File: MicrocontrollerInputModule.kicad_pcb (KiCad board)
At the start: 2 copper layers, 33.8 x 131 mm, 359 parts, among them J1 Conn_02x04_Odd_Even, SW1 KXT3, SW2 KXT3, U1 W25Q16JVUXIQ, U2 RP2040, U3 TXB0108DQSR, U4 TXB0108DQSR, Y1 12.000MHz

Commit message: Add files via upload
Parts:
- removed the G*** at (73.0, 68.0)
- added G***: LOGO, InputModule:heart, B.Cu at (67.0, 178.9)
- moved C15 13.0 mm to (54.8, 148.8), turned to 90 degrees
- moved R4 12.5 mm to (65.2, 144.2), turned to 0 degrees
- moved C19 12.2 mm to (56.9, 144.3), turned to -90 degrees
- moved R9 6.91 mm to (59.9, 139.2), turned to 45 degrees
- moved G*** 6.40 mm to (72.9, 78.6)
- moved G*** 4.30 mm to (72.9, 105.7)
- moved R8 3.94 mm to (58.6, 153.4)
- moved C20 3.79 mm to (62.6, 140.9)
- moved C17 2.54 mm to (60.7, 154.5), turned to -90 degrees
- moved D2 0.60 mm to (68.0, 153.2), turned to -135 degrees
- moved C14 0.17 mm to (65.2, 146.2)
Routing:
- net /BOARD_ID: track 41.9 -> 22.1 mm, vias 2 -> 3
- net +5V: track 35.8 -> 50.6 mm, vias 19 -> 21
- net /~{RESET}: track 60.4 -> 48.9 mm, vias 2 -> 1
- net GND: track 1066.5 -> 1077.0 mm, vias 103 -> 116
- net Net-(U4-OE): track 13.6 -> 4.24 mm, vias 2 -> 0
- net Net-(R1-Pad1): track 24.4 -> 16.4 mm
- net +3V3: track 112.4 -> 116.7 mm, vias 6 -> 4
- net Net-(U3-OE): track 5.81 -> 1.60 mm, vias 2 -> 0
- net /XIN: track 8.07 -> 10.1 mm
- net Net-(N261-DOUT): track 39.5 -> 37.9 mm
- net /D8: track 16.6 -> 15.4 mm
- net /NeopixelMatrix/STRIP16: track 8.28 -> 7.54 mm
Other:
- board text added: "LED Strip RP2040 Pin Guide:"
- board text added: "LED Strip | GPIO Pin 1 | D23 2 | D22 3 | D21 4 | D17 5 | D16 6 | D15 7 | D14 8 | D13"
- board text added: "LED Strip | GPIO Pin 9 | D12 10 | D11 11 | D10 12 | D9 13 | D8 14 | D7 15 | D6 16 | D5"
- board text added: "LGBTQIA+"
- board text removed: "Check out the Young Amateurs Radio Club for a safe space to learn and experiment with amateur radio!"

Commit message: Version 2
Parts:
- removed C19, C20: 0.1uF, Capacitor_SMD:C_0603_1608Metric
- removed H1, H2: 24929, InputModule:MountingHole_3.7mm_Pad_24929
- removed H3, H4: MountingHole, MountingHole:MountingHole_2.1mm
- removed J1: Conn_02x04_Odd_Even, InputModule:PogoPads_2x4_P2.0mm
- added F1: Polyfuse 600mA, Resistor_SMD:R_1206_3216Metric, B.Cu at (102.9, 149.0)
- added F2: Polyfuse 200mA, Resistor_SMD:R_1206_3216Metric, B.Cu at (110.3, 153.1)
- added J2: FH34SRJ-12S-0.5SH_50_, FH34SRJ-12S-0.5SH_50_:HRS_FH34SRJ-12S-0.5SH_50_, B.Cu at (103.2, 152.5)
- added R10: 470, Resistor_SMD:R_0402_1005Metric, B.Cu at (95.4, 137.0)
- added R11: 470, Resistor_SMD:R_0402_1005Metric, B.Cu at (94.8, 139.6)
- added R12: 470, Resistor_SMD:R_0402_1005Metric, B.Cu at (92.2, 142.1)
- added R13: 470, Resistor_SMD:R_0402_1005Metric, B.Cu at (91.2, 146.7)
- added R14: 470, Resistor_SMD:R_0402_1005Metric, B.Cu at (94.9, 147.6)
- added R15: 470, Resistor_SMD:R_0402_1005Metric, B.Cu at (94.9, 150.0)
- added R16: 470, Resistor_SMD:R_0402_1005Metric, B.Cu at (92.2, 152.0)
- added R17: 0, Resistor_SMD:R_0402_1005Metric, F.Cu at (117.2, 61.3)
- added R18: 0, Resistor_SMD:R_0402_1005Metric, F.Cu at (117.2, 74.9)
- added R19: 0, Resistor_SMD:R_0402_1005Metric, F.Cu at (117.3, 88.6)
- added R20: 0, Resistor_SMD:R_0402_1005Metric, F.Cu at (117.2, 102.3)
- added R21: 0, Resistor_SMD:R_0402_1005Metric, F.Cu at (117.2, 116.1)
- added R22: 0, Resistor_SMD:R_0402_1005Metric, F.Cu at (117.2, 129.8)
- added R23: 0, Resistor_SMD:R_0402_1005Metric, F.Cu at (117.2, 143.5)
- added R24: 10k, Resistor_SMD:R_0402_1005Metric, B.Cu at (109.7, 146.0)
- C17, C18: value 0.1uF -> 10uF
- C21, C22, C23, C24, C25, C26, C27, C28, C29, C30, C31, C32, C33, C34, C35, C36: footprint Capacitor_SMD:C_0402_1005Metric -> Capacitor_SMD:C_0603_1608Metric
- R8: value 10K -> 10k
- R9: value 10K -> 470
- SW1, SW2: moved to B.Cu
- U3, U4: value TXB0108DQSR -> 74AHC125BQ_115; footprint FootprintLibrary:USON-20_2x4mm_P0.4mm -> 74AHC125BQ_115:QFN50P300X250X100-15N
- moved G*** 145.2 mm to (209.6, 151.6)
- moved G*** 145.2 mm to (203.6, 139.7)
- moved G*** 145.2 mm to (194.6, 139.7)
- moved G*** 145.2 mm to (215.6, 100.7)
- moved G*** 145.2 mm to (200.6, 139.7)
- moved G*** 145.2 mm to (197.6, 139.7)
- moved G*** 145.2 mm to (206.9, 140.1)
- moved G*** 111.2 mm to (176.6, 65.7)
- moved G*** 108.5 mm to (176.6, 46.7)
- moved C15 51.9 mm to (106.7, 149.4), turned to 0 degrees
- moved SW2 51.8 mm to (100.5, 136.9), turned to 0 degrees
- moved R8 50.1 mm to (108.2, 146.4), turned to 90 degrees
- moved SW1 44.2 mm to (115.2, 149.8), turned to 90 degrees
- moved C1 40.7 mm to (102.3, 142.5), turned to 180 degrees
- moved C9 39.6 mm to (116.0, 140.5)
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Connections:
- C17 pad 1: +3V3 -> +5V
- C18 pad 1: GND -> +5V
- C18 pad 2: +5V -> GND
- N127 pad 4: /NeopixelMatrix/STRIP8 -> /NeopixelMatrix/END-STRIP7
- N163 pad 4: /NeopixelMatrix/STRIP10 -> /NeopixelMatrix/END-STRIP19
- N19 pad 4: /NeopixelMatrix/STRIP2 -> /NeopixelMatrix/END-STRIP1
- N199 pad 4: /NeopixelMatrix/STRIP12 -> /NeopixelMatrix/END-STRIP11
- N235 pad 4: /NeopixelMatrix/STRIP14 -> /NeopixelMatrix/END-STRIP13
- N271 pad 4: /NeopixelMatrix/STRIP16 -> /NeopixelMatrix/END-STRIP15
- N55 pad 4: /NeopixelMatrix/STRIP4 -> /NeopixelMatrix/END-STRIP3
- N91 pad 4: /NeopixelMatrix/STRIP6 -> /NeopixelMatrix/END-STRIP5
- R8 pad 1: Net-(U3-OE) -> GND
- R8 pad 2: +3V3 -> /D7
- R9 pad 1: Net-(U4-OE) -> Net-(U3-1Y)
- R9 pad 2: +3V3 -> /NeopixelMatrix/STRIP1
- U2 pad 27: /D16 -> unconnected-(U2-GPIO16-Pad27)
- U2 pad 28: /D17 -> unconnected-(U2-GPIO17-Pad28)
- U2 pad 32: /D21 -> unconnected-(U2-GPIO21-Pad32)
- U2 pad 34: /D22 -> unconnected-(U2-GPIO22-Pad34)
- U2 pad 35: /D23 -> unconnected-(U2-GPIO23-Pad35)
- U2 pad 7: /D5 -> unconnected-(U2-GPIO5-Pad7)
- U2 pad 8: /D6 -> Net-(U2-GPIO6)
- U3 pad 1: /D12 -> Net-(U2-GPIO6)
- U3 pad 10: /D5 -> /D7
- U3 pad 11: /NeopixelMatrix/STRIP16 -> Net-(U3-4Y)
- U3 pad 12: /NeopixelMatrix/STRIP15 -> /D12
- U3 pad 13: /NeopixelMatrix/STRIP14 -> /D7
- U3 pad 14: /NeopixelMatrix/STRIP13 -> +5V
- U3 pad 2: /D11 -> /D15
- U3 pad 3: /D10 -> Net-(U3-1Y)
- U3 pad 4: /D9 -> /D7
- U3 pad 5: +3V3 -> /D14
- U3 pad 6: Net-(U3-OE) -> Net-(U3-2Y)
- U3 pad 7: /D8 -> GND
- U3 pad 8: /D7 -> Net-(U3-3Y)
- U3 pad 9: /D6 -> /D13
- U4 pad 1: /D23 -> /D7
- U4 pad 10: /D13 -> /D7
- U4 pad 11: /NeopixelMatrix/STRIP8 -> Net-(U4-4Y)
- U4 pad 12: /NeopixelMatrix/STRIP7 -> /D8
- U4 pad 13: /NeopixelMatrix/STRIP6 -> /D7
- U4 pad 14: /NeopixelMatrix/STRIP5 -> +5V
- U4 pad 2: /D22 -> /D11
- U4 pad 3: /D21 -> Net-(U4-1Y)
- U4 pad 4: /D17 -> /D7
- U4 pad 5: +3V3 -> /D10
- U4 pad 6: Net-(U4-OE) -> Net-(U4-2Y)
- U4 pad 7: /D16 -> GND
- U4 pad 8: /D15 -> Net-(U4-3Y)
- U4 pad 9: /D14 -> /D9
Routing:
- net /NeopixelMatrix/STRIP2: track 81.1 -> 0.00 mm, vias 1 -> 0
- net /NeopixelMatrix/STRIP4: track 66.6 -> 0.00 mm, vias 1 -> 0
- net Net-(U2-GPIO6): track 0.00 -> 55.4 mm, vias 0 -> 2
- net +3V3: track 116.7 -> 61.7 mm, vias 4 -> 0
- net /NeopixelMatrix/STRIP6: track 50.9 -> 0.00 mm, vias 1 -> 0
- net /~{RESET}: track 48.9 -> 4.24 mm, vias 1 -> 0
- net +5V: track 50.6 -> 7.03 mm, vias 21 -> 1
- net /NeopixelMatrix/STRIP7: track 44.4 -> 87.5 mm
- net /NeopixelMatrix/STRIP5: track 58.5 -> 99.9 mm, vias 1 -> 3
- net /NeopixelMatrix/STRIP11: track 28.9 -> 66.2 mm, vias 1 -> 5
- net /NeopixelMatrix/STRIP8: track 36.9 -> 0.00 mm, vias 1 -> 0
- net /NeopixelMatrix/STRIP15: track 4.15 -> 41.0 mm, vias 1 -> 3
- net /NeopixelMatrix/STRIP10: track 35.6 -> 0.00 mm, vias 1 -> 0
- net /NeopixelMatrix/STRIP3: track 73.9 -> 108.0 mm, vias 1 -> 3
- net /NeopixelMatrix/END-STRIP13: track 0.00 -> 33.6 mm
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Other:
- board size 33.8 x 131 mm -> 31 x 111.4 mm

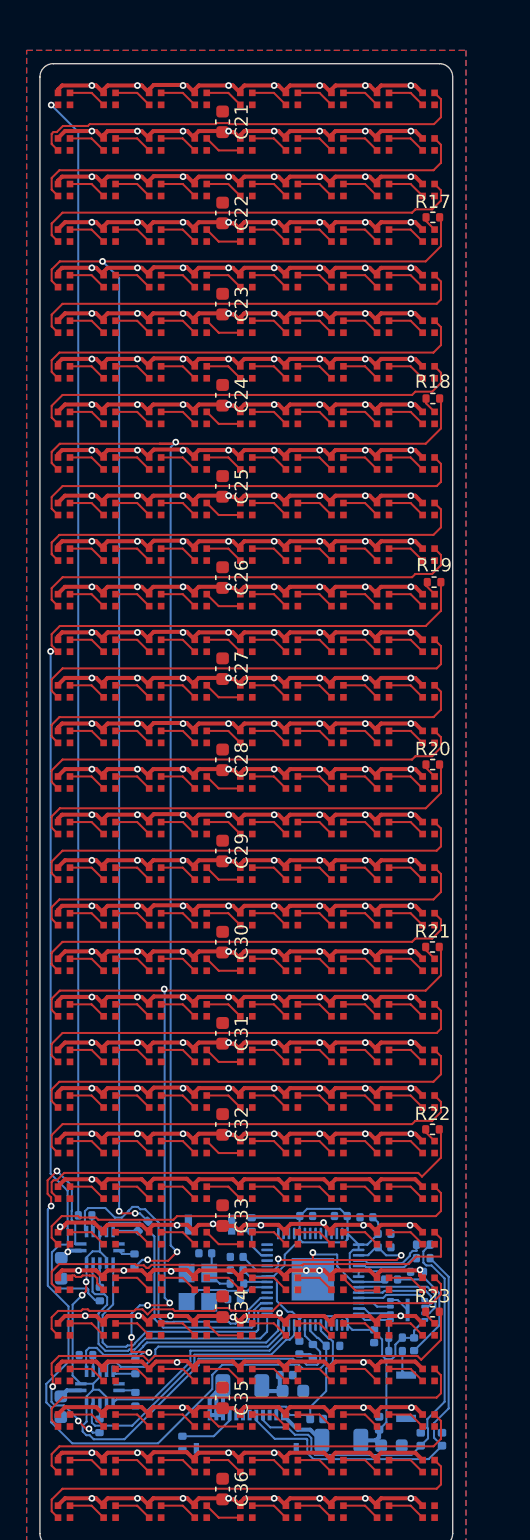
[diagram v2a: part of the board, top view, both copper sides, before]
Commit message: All traces ran. Zero DRC errors.
Most of the DRC warnings can be ignored since they involve the LEDs and their footprints not including a certain layer or label.
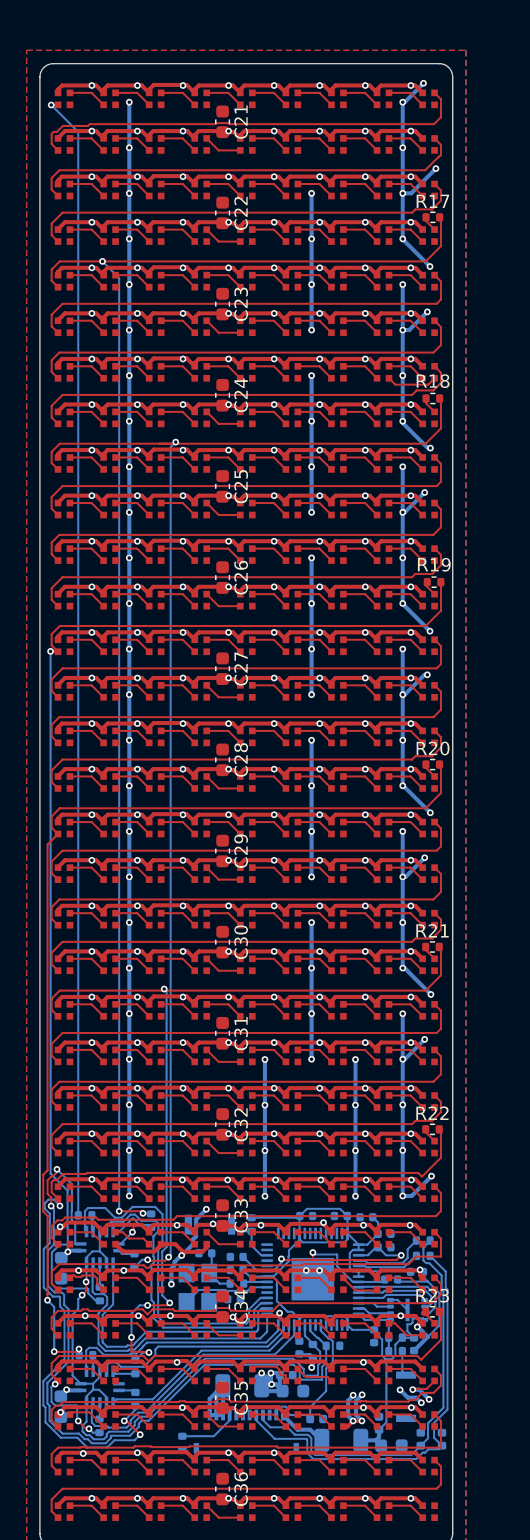
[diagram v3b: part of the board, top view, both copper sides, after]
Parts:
- moved R10 0.73 mm to (96.1, 136.6), turned to 90 degrees
- moved R6 0.31 mm to (116.5, 138.1)
- moved R5 0.17 mm to (116.5, 139.3)
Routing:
- net +5V: track 7.03 -> 296.8 mm, vias 1 -> 107
- net /NeopixelMatrix/STRIP9: track 33.7 -> 75.8 mm, vias 0 -> 3
- net /NeopixelMatrix/STRIP13: track 33.9 -> 65.8 mm, vias 0 -> 3
- net GND: track 1043.9 -> 1050.3 mm, vias 229 -> 239
- net Net-(U2-GPIO6): track 55.4 -> 57.4 mm
- net /D14: track 20.9 -> 22.6 mm
- net Net-(U3-2Y): track 1.90 -> 3.53 mm
- net /D7: track 46.0 -> 47.4 mm
- net +3V3: track 61.7 -> 63.0 mm
- net /D15: track 25.1 -> 25.9 mm
- net Net-(N257-DOUT): track 2.90 -> 3.45 mm
- net /NeopixelMatrix/END-STRIP15: track 33.3 -> 33.8 mm
- net /NeopixelMatrix/STRIP5: track 99.9 -> 99.3 mm

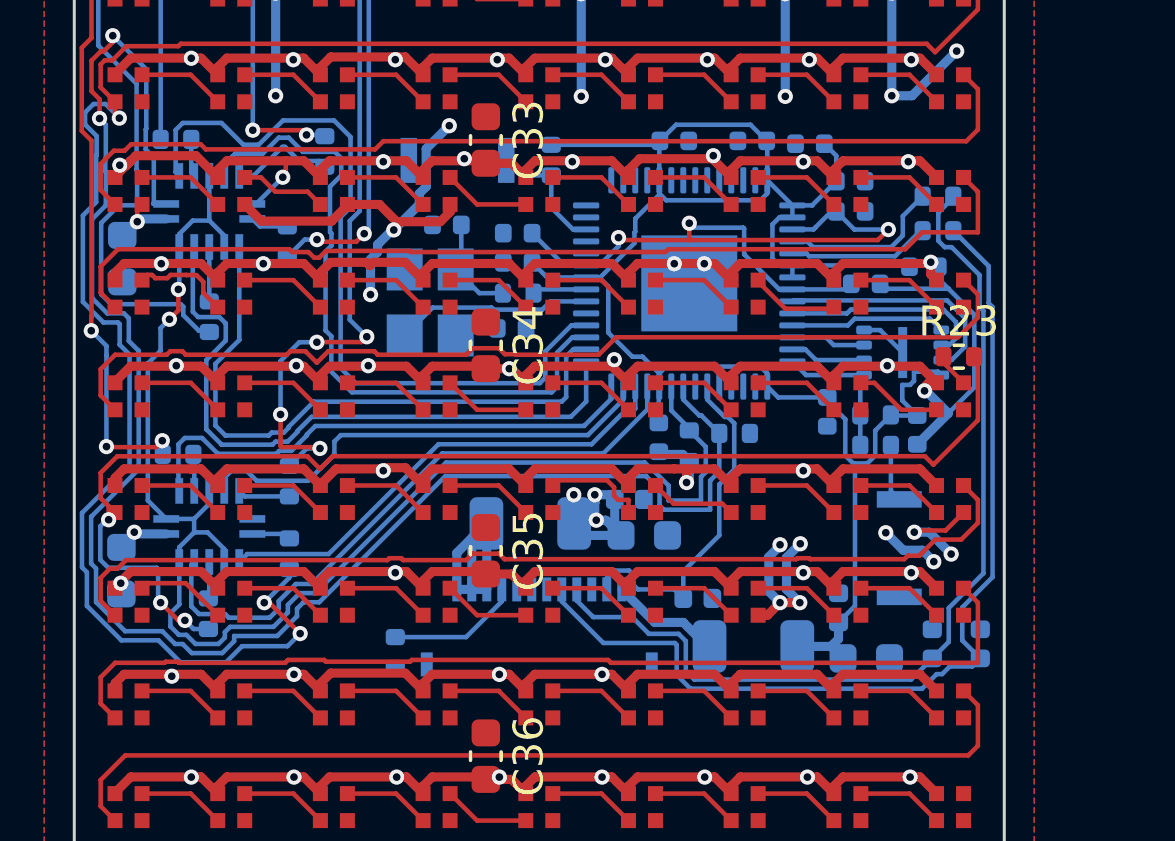
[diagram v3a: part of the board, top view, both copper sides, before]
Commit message: Fixed some routing issues for better Ground connections
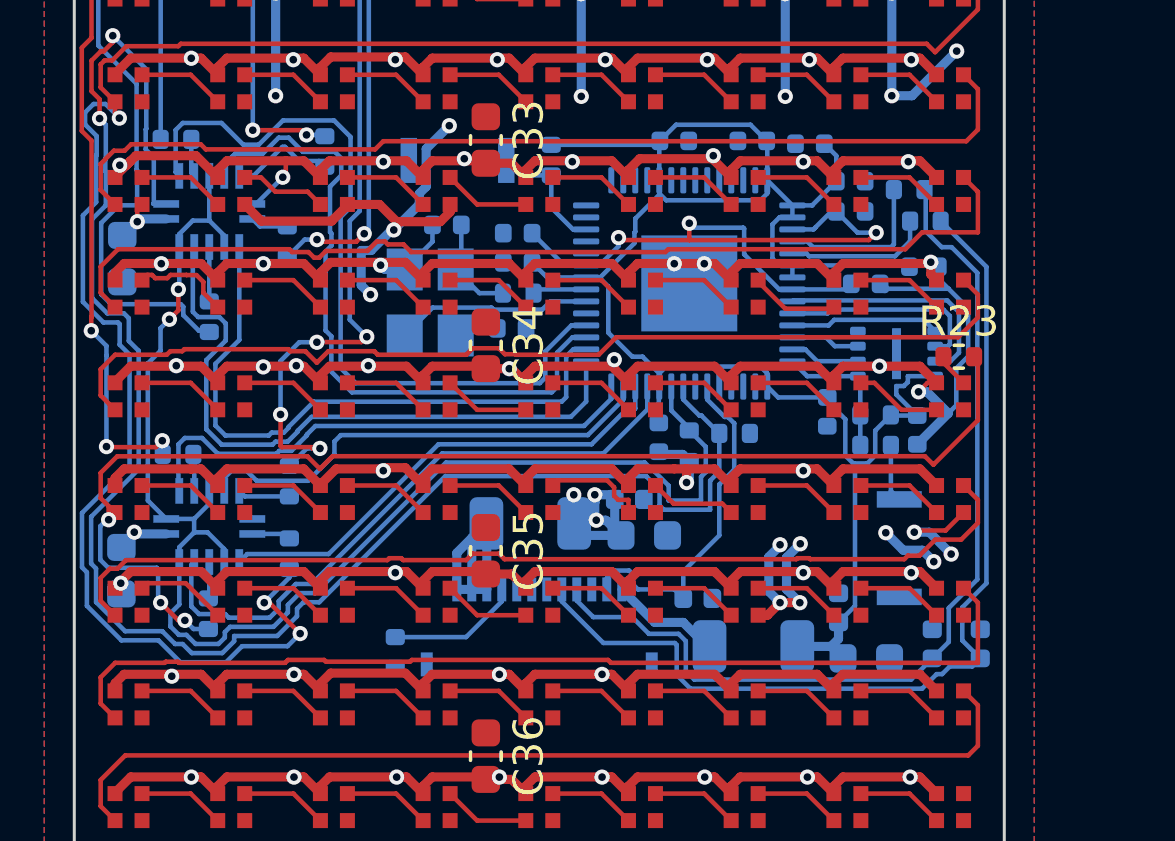
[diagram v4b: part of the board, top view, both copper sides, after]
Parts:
- moved R6 0.98 mm to (115.5, 137.9)
- moved R5 0.53 mm to (116.1, 138.9)
- moved U1 0.21 mm to (115.1, 143.4)
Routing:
- net GND: track 1050.3 -> 1051.6 mm, vias 239 -> 241
- net +1V1: track 24.2 -> 23.4 mm
